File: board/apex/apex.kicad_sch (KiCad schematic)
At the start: 5 parts, among them J1 USB_C_Receptacle_PowerOnly_6P

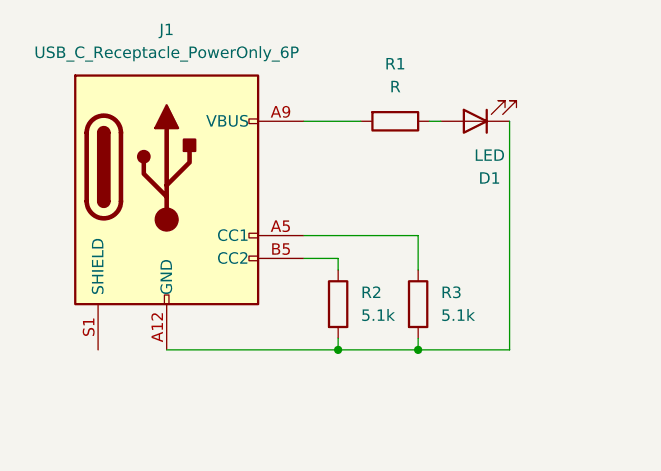
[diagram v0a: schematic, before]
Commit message: testing adding usb 3D model
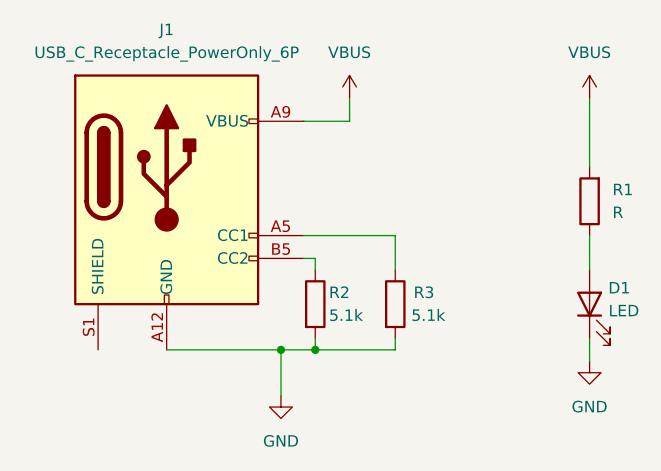
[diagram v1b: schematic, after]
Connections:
- net GND: now reaches D1.1 (K), J1.A12 (GND), J1.B12 (GND), R2.2, R3.2
- net VBUS: now reaches J1.A9 (VBUS), J1.B9 (VBUS), R1.2
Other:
- company: (none) -> DelgadoTechnologies
- title: (none) -> Test1
- moved on the sheet: D1, R1, R2, R3

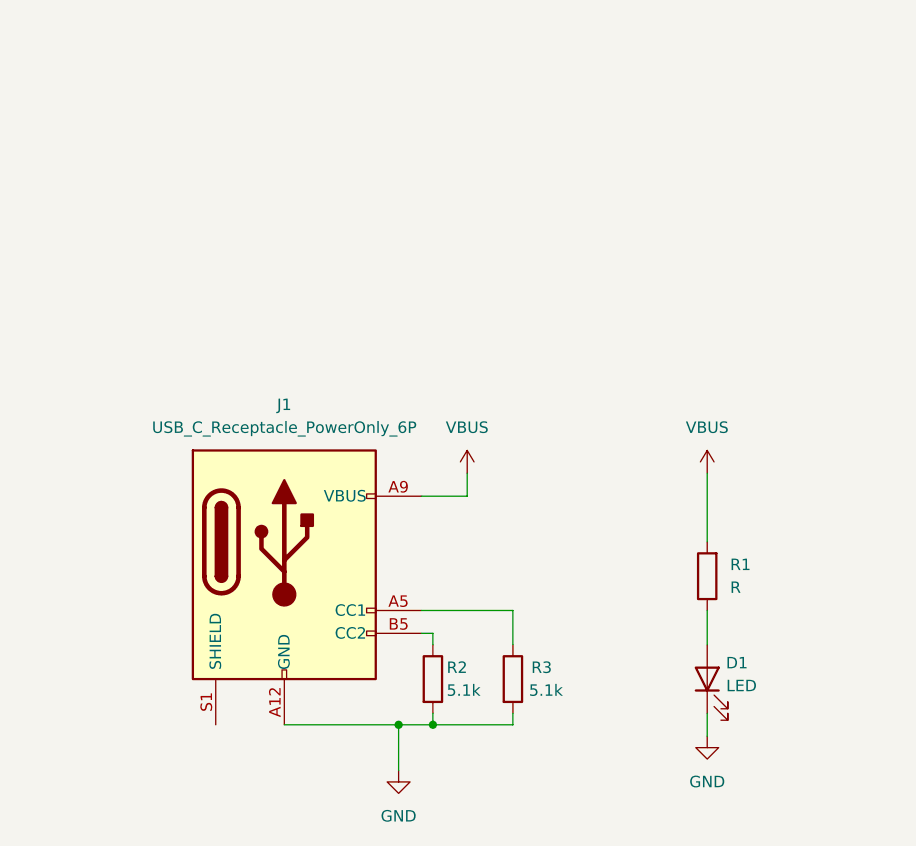
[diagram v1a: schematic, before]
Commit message: added power input/outputs
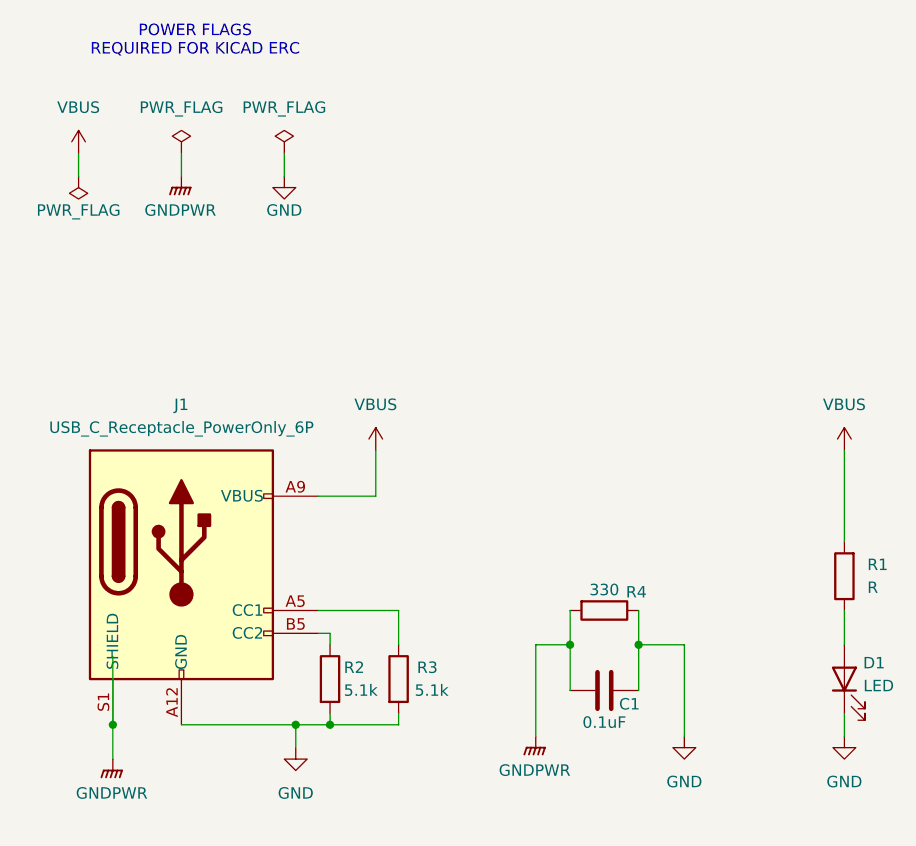
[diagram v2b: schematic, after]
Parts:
- added C1: 0.1uF, symbol Device:C
- added R4: 330, symbol Device:R
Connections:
- net GND: now also C1.1, R4.1
- net GNDPWR: now reaches J1.S1 (SHIELD)
- net GNDPWR: now also C1.2, R4.2
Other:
- note added: "POWER FLAGS REQUIRED FOR KICAD ERC"
- moved on the sheet: D1, J1, R1, R2, R3

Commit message: added SMDs to board
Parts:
- C1: footprint (none) -> Capacitor_SMD:C_0805_2012Metric
- D1: footprint (none) -> LED_SMD:LED_0805_2012Metric
- J1: footprint (none) -> Connector_USB:USB_C_Receptacle_GCT_USB4125-xx-x-0190_6P_TopMnt_Horizontal
- R1, R2, R3, R4: footprint (none) -> Resistor_SMD:R_0805_2012Metric
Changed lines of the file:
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@@
 			)
 		)
-		(property "Footprint" ""
+		(property "Footprint" "LED_SMD:LED_0805_2012Metric"
 			(at 102.87 87.63 0)
 			(effects
@@
 			)
 		)
-		(property "Footprint" ""
+		(property "Footprint" "Resistor_SMD:R_0805_2012Metric"
 			(at 51.562 87.63 90)
 			(effects
@@
 			)
 		)
-		(property "Footprint" ""
+		(property "Footprint" "Resistor_SMD:R_0805_2012Metric"
 			(at 43.942 87.63 90)
 			(effects
@@
 			)
 		)
-		(property "Footprint" ""
+		(property "Footprint" "Resistor_SMD:R_0805_2012Metric"
 			(at 104.648 76.2 90)
 			(effects
@@
 			)
 		)
-		(property "Footprint" ""
+		(property "Footprint" "Resistor_SMD:R_0805_2012Metric"
 			(at 76.2 78.232 90)
 			(effects
@@
 			)
 		)
-		(property "Footprint" ""
+		(property "Footprint" "Connector_USB:USB_C_Receptacle_GCT_USB4125-xx-x-0190_6P_TopMnt_Horizontal"
 			(at 33.02 72.39 0)
 			(effects
@@
 			)
 		)
-		(property "Footprint" ""
+		(property "Footprint" "Capacitor_SMD:C_0805_2012Metric"
 			(at 72.39 89.8652 0)
 			(effects

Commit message: added models
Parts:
- added C2, C3: 10 uF, Capacitor_SMD:C_0805_2012Metric, symbol Device:C
- added U1: AP7363-33D-13, TO252-3L_DIO, symbol AP7363_33D_13:AP7363-33D-13
- C1: value 0.1uF -> 0.1 uF
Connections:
- net GND: now also C2.1, C3.1, U1.2 (GND)
- net VBUS: now also C2.2, U1.1 (IN); no longer R1.2
- new net: C3.2, R1.2, U1.3 (OUT)
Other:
- moved on the sheet: D1, R1

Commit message: organized modules
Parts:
- removed D1: LED, LED_SMD:LED_0805_2012Metric, symbol Device:LED
- removed J1: USB_C_Receptacle_PowerOnly_6P, Connector_USB:USB_C_Receptacle_GCT_USB4125-xx-x-0190_6P_TopMnt_Horizontal, symbol Connector:USB_C_Receptacle_PowerOnly_6P
- added J1: USB4125-GF-A_REVA2, USB4125-GF-A_REVA2:GCT_USB4125-GF-A_REVA2, symbol USB4125-GF-A_REVA2:USB4125-GF-A_REVA2
- added LED1: 150080BS75000, LED_BS75000_WRE, symbol 150080BS75000:150080BS75000
- R1: value R -> 3.3
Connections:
- net GND: now also J1.A12 (GND), J1.B12 (GND__1), LED1.1
- net GNDPWR: now also J1.S1 (SHIELD), J1.S2 (SHIELD__1), J1.S3 (SHIELD__2), J1.S4 (SHIELD__3)
- net VBUS: now also J1.A9 (VBUS), J1.B9 (VBUS__1)
- net +3V3: now reaches C3.2, R1.2, U1.3 (OUT)
- net at R1.1: now also LED1.2
- net at R3.1: now also J1.A5 (CC1)
- net at R2.1: now also J1.B5 (CC2)
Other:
- moved on the sheet: C2, C3, R1, U1

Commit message: updated schematic
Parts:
- J1: footprint USB4125-GF-A_REVA2:GCT_USB4125-GF-A_REVA2 -> USB4125_GF_A:GCT_USB4125-GF-A_REVA2
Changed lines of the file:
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@@
 			)
 		)
-		(property "Footprint" "USB4125-GF-A_REVA2:GCT_USB4125-GF-A_REVA2"
+		(property "Footprint" "USB4125_GF_A:GCT_USB4125-GF-A_REVA2"
 			(at 21.59 68.58 0)
 			(effects

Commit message: checked parity with schematic
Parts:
- added H1: H1_MH, MountingHole:MountingHole_2.5mm_Pad, symbol Mechanical:MountingHole
- added H2: H2_MH, MountingHole:MountingHole_2.5mm_Pad, symbol Mechanical:MountingHole
- added H3: H3_MH, MountingHole:MountingHole_2.5mm_Pad, symbol Mechanical:MountingHole
- added H4: H4_MH, MountingHole:MountingHole_2.5mm_Pad, symbol Mechanical:MountingHole
- LED1: footprint LED_BS75000_WRE -> LEDBS75000_WRE:LED_BS75000_WRE
- U1: footprint TO252-3L_DIO -> AP7363_33D_13:TO252-3L_DIO

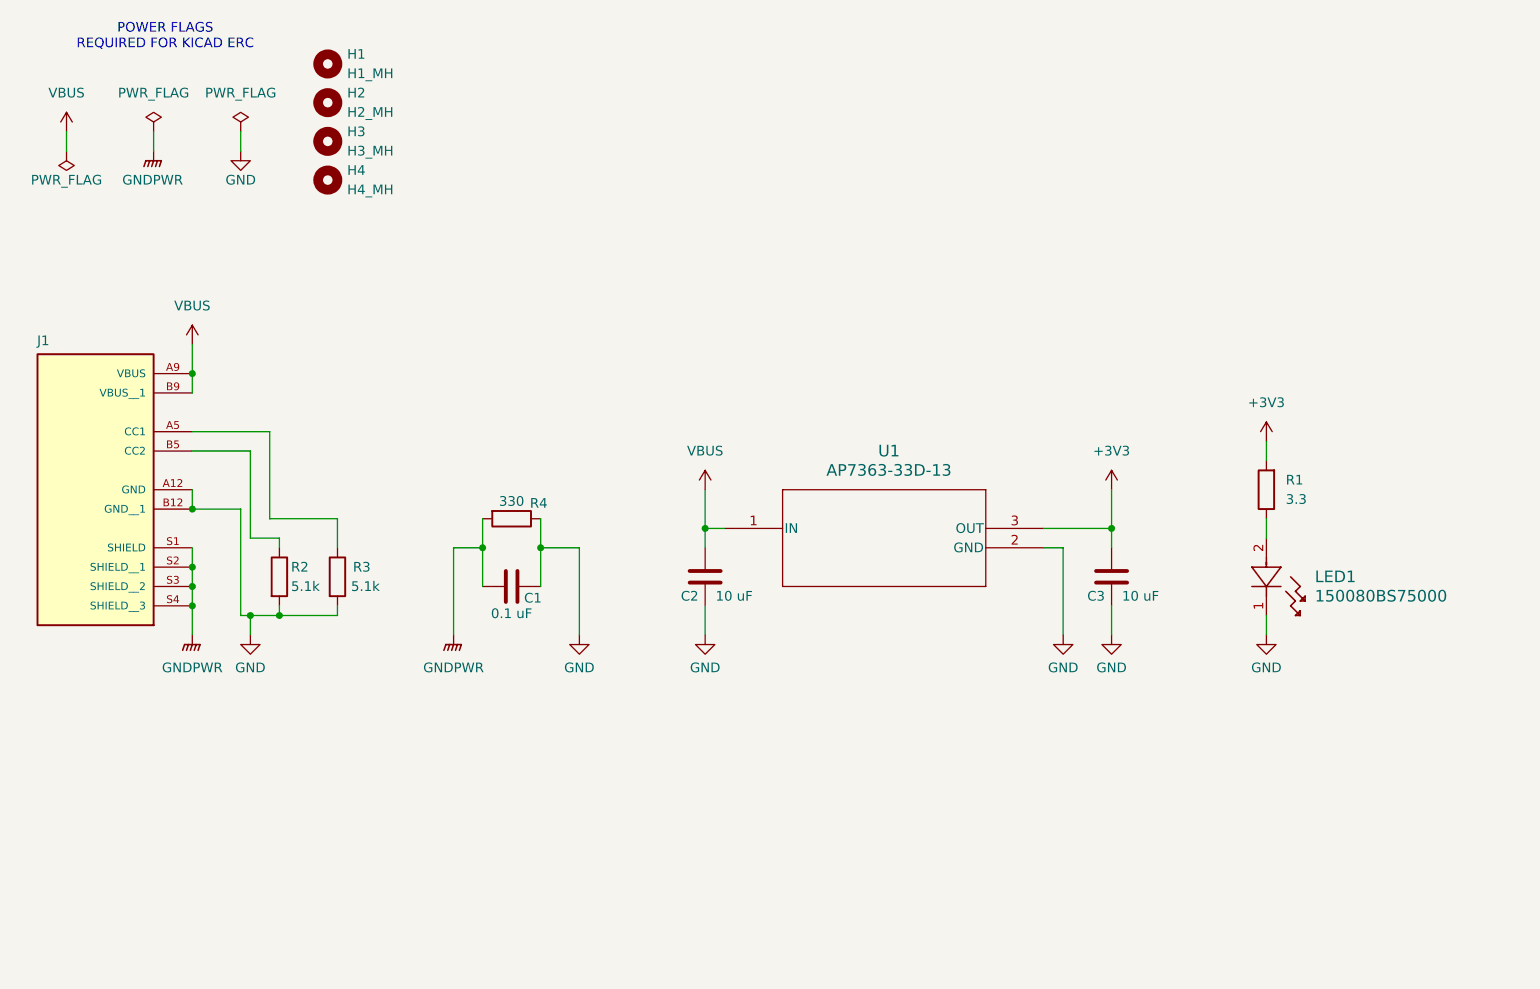
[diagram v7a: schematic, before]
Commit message: added 3d models; added TVS diodes
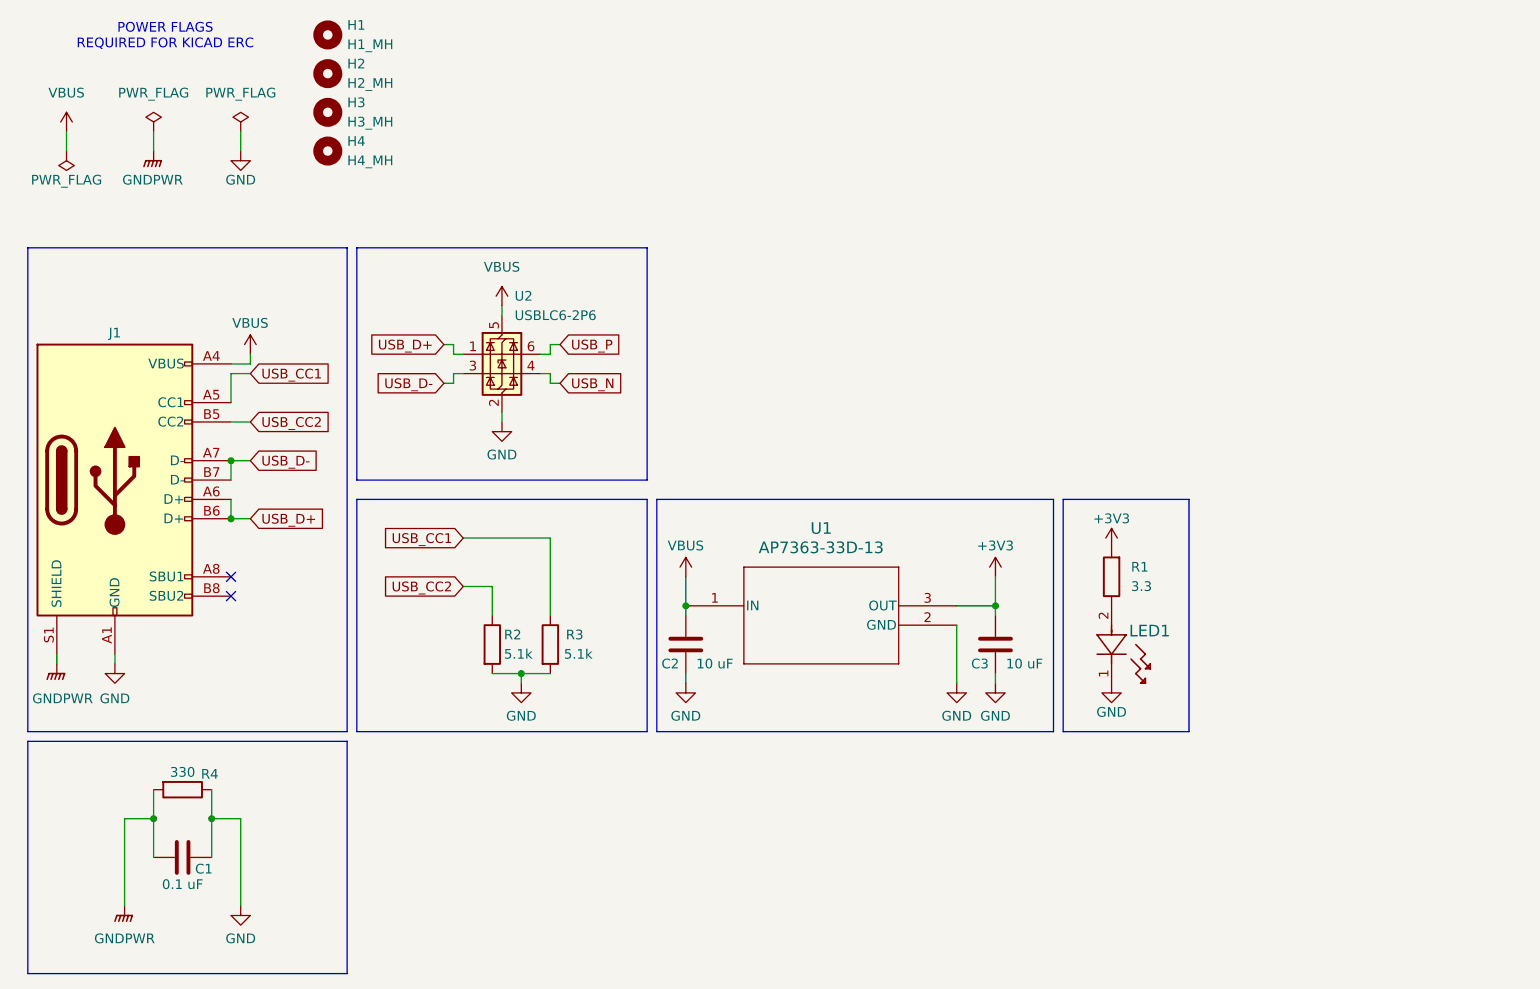
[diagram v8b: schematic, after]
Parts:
- removed J1: USB4125-GF-A_REVA2, USB4125_GF_A:GCT_USB4125-GF-A_REVA2, symbol USB4125-GF-A_REVA2:USB4125-GF-A_REVA2
- added J1: USB_C_Receptacle_USB2.0_16P, Connector_USB:USB_C_Receptacle_GCT_USB4110, symbol Connector:USB_C_Receptacle_USB2.0_16P
- added U2: USBLC6-2P6, Package_TO_SOT_SMD:SOT-666, symbol Power_Protection:USBLC6-2P6
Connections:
- net GND: now also J1.A1 (GND), J1.A12 (GND), J1.B1 (GND), J1.B12 (GND), U2.2 (GND)
- net GNDPWR: now also J1.S1 (SHIELD)
- net VBUS: now also J1.A4 (VBUS), J1.A9 (VBUS), J1.B4 (VBUS), J1.B9 (VBUS), U2.5 (VBUS)
- net USB_CC1: now reaches R3.1
- net USB_CC1: now also J1.A5 (CC1)
- net USB_CC2: now reaches R2.1
- net USB_CC2: now also J1.B5 (CC2)
- new net USB_D+: J1.A6 (D+), J1.B6 (D+), U2.1 (I/O1)
- new net USB_D-: J1.A7 (D-), J1.B7 (D-), U2.3 (I/O2)
- new net USB_N: U2.4 (I/O2)
- new net USB_P: U2.6 (I/O1)
- no-connect marks 0 -> 2
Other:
- moved on the sheet: C1, C2, C3, H1, H2, H3, H4, LED1, R1, R2, R3, R4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
